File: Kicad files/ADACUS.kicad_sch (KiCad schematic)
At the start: 0 parts

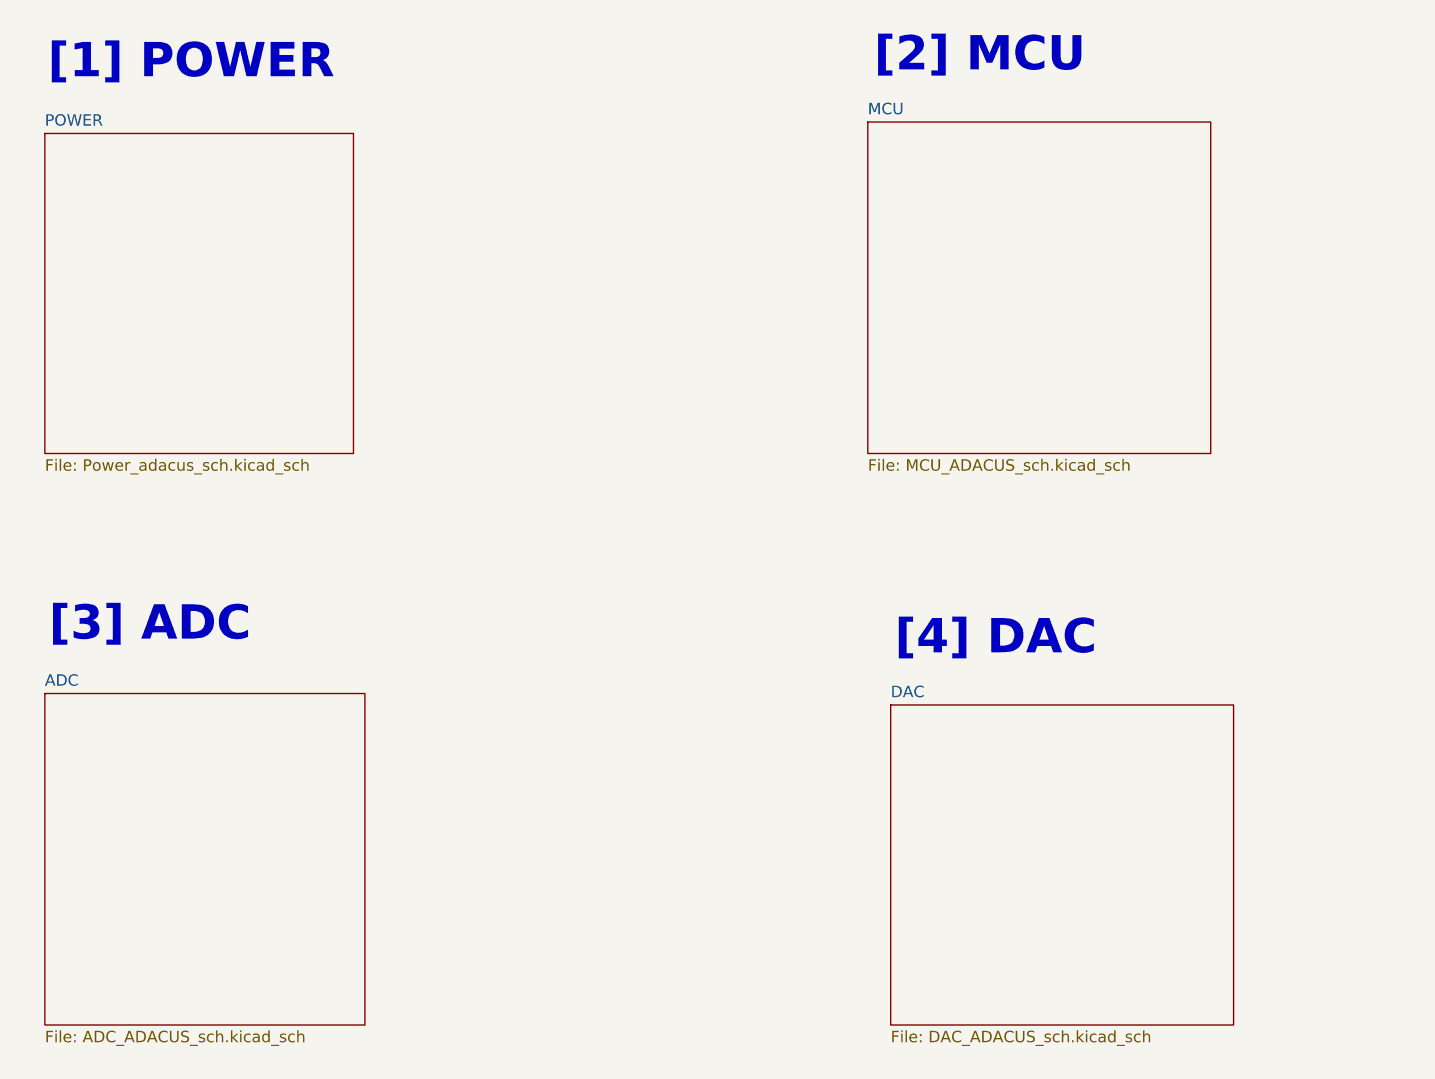
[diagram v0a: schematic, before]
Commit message: [FILE] Finished board
Added PCB documents and finished schematics. Project is now done with both Altium and Kicad files uploaded
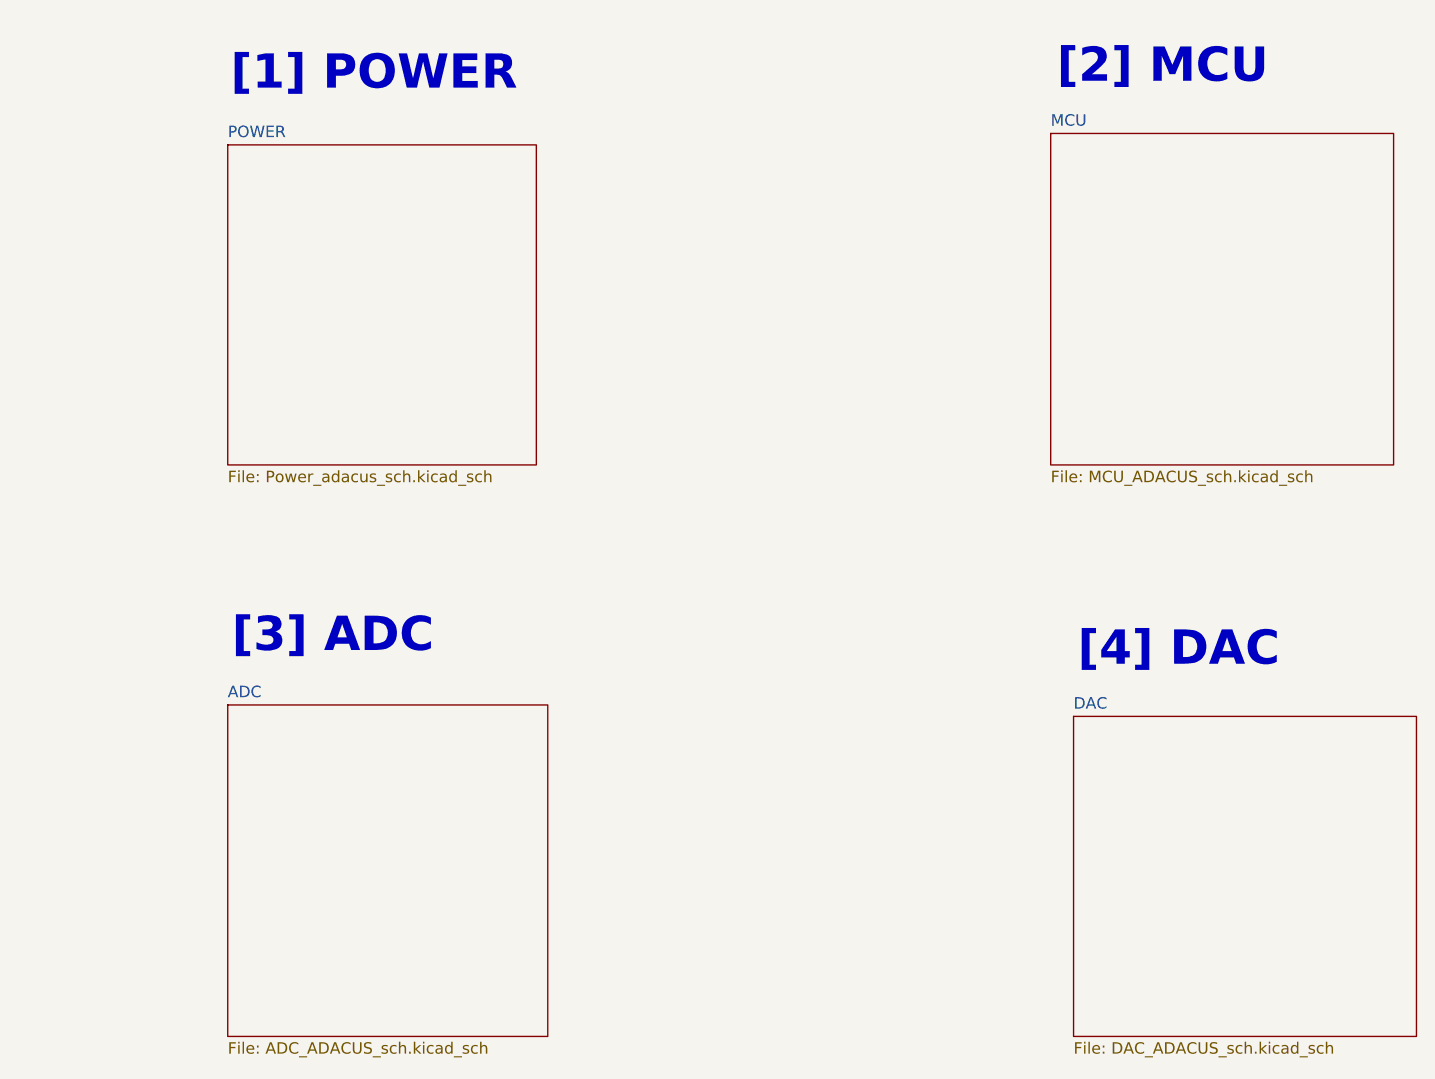
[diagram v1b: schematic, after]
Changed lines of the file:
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@@
 	(text "[2] MCU"
 		(exclude_from_sim yes)
-		(at 161.036 34.544 0)
+		(at 181.356 35.814 0)
 		(effects
 			(font
@@
 	(text "[3] ADC"
 		(exclude_from_sim yes)
-		(at 68.834 97.79 0)
+		(at 89.154 99.06 0)
 		(effects
 			(font
@@
 	(text "[4] DAC\n"
 		(exclude_from_sim yes)
-		(at 162.814 99.314 0)
+		(at 183.134 100.584 0)
 		(effects
 			(font
@@
 	(text "[1] POWER"
 		(exclude_from_sim yes)
-		(at 73.406 35.306 0)
+		(at 93.726 36.576 0)
 		(effects
 			(font
@@
 	)
 	(sheet
-		(at 151.13 106.68)
+		(at 171.45 107.95)
 		(size 38.1 35.56)
 		(fields_autoplaced yes)
@@
 		)
 		(property "Sheetname" "DAC"
-			(at 151.13 105.9684 0)
+			(at 171.45 107.2384 0)
 			(effects
 				(font
@@
 		)
 		(property "Sheetfile" "DAC_ADACUS_sch.kicad_sch"
-			(at 151.13 142.8246 0)
+			(at 171.45 144.0946 0)
 			(effects
 				(font
@@
 	)
 	(sheet
-		(at 57.15 43.18)
+		(at 77.47 44.45)
 		(size 34.29 35.56)
 		(fields_autoplaced yes)
@@
 		)
 		(property "Sheetname" "POWER"
-			(at 57.15 42.4684 0)
+			(at 77.47 43.7384 0)
 			(effects
 				(font
@@
 		)
 		(property "Sheetfile" "Power_adacus_sch.kicad_sch"
-			(at 57.15 79.3246 0)
+			(at 77.47 80.5946 0)
 			(effects
 				(font
@@
 	)
 	(sheet
-		(at 57.15 105.41)
+		(at 77.47 106.68)
 		(size 35.56 36.83)
 		(fields_autoplaced yes)
@@
 		)
 		(property "Sheetname" "ADC"
-			(at 57.15 104.6984 0)
+			(at 77.47 105.9684 0)
 			(effects
 				(font
@@
 		)
 		(property "Sheetfile" "ADC_ADACUS_sch.kicad_sch"
-			(at 57.15 142.8246 0)
+			(at 77.47 144.0946 0)
 			(effects
 				(font
@@
 	)
 	(sheet
-		(at 148.59 41.91)
+		(at 168.91 43.18)
 		(size 38.1 36.83)
 		(fields_autoplaced yes)
@@
 		)
 		(property "Sheetname" "MCU"
-			(at 148.59 41.1984 0)
+			(at 168.91 42.4684 0)
 			(effects
 				(font
@@
 		)
 		(property "Sheetfile" "MCU_ADACUS_sch.kicad_sch"
-			(at 148.59 79.3246 0)
+			(at 168.91 80.5946 0)
 			(effects
 				(font
